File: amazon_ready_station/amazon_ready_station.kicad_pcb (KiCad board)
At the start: 2 copper layers, 35.1 x 65.2 mm, 30 parts, among them J7 BRKOUT_LEFT, J8 BRKOUT_RIGHT, Q1 2N2219

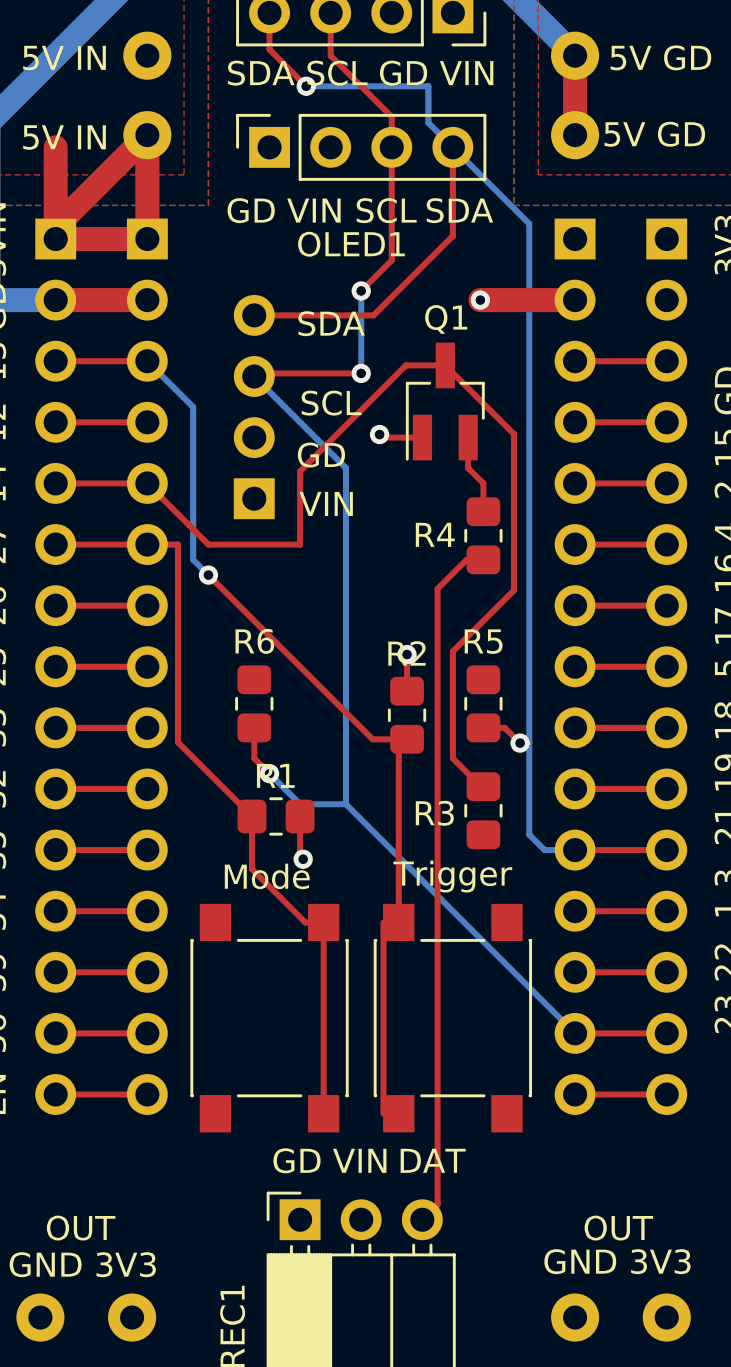
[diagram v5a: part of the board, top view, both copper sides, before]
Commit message: pcb with receiver components
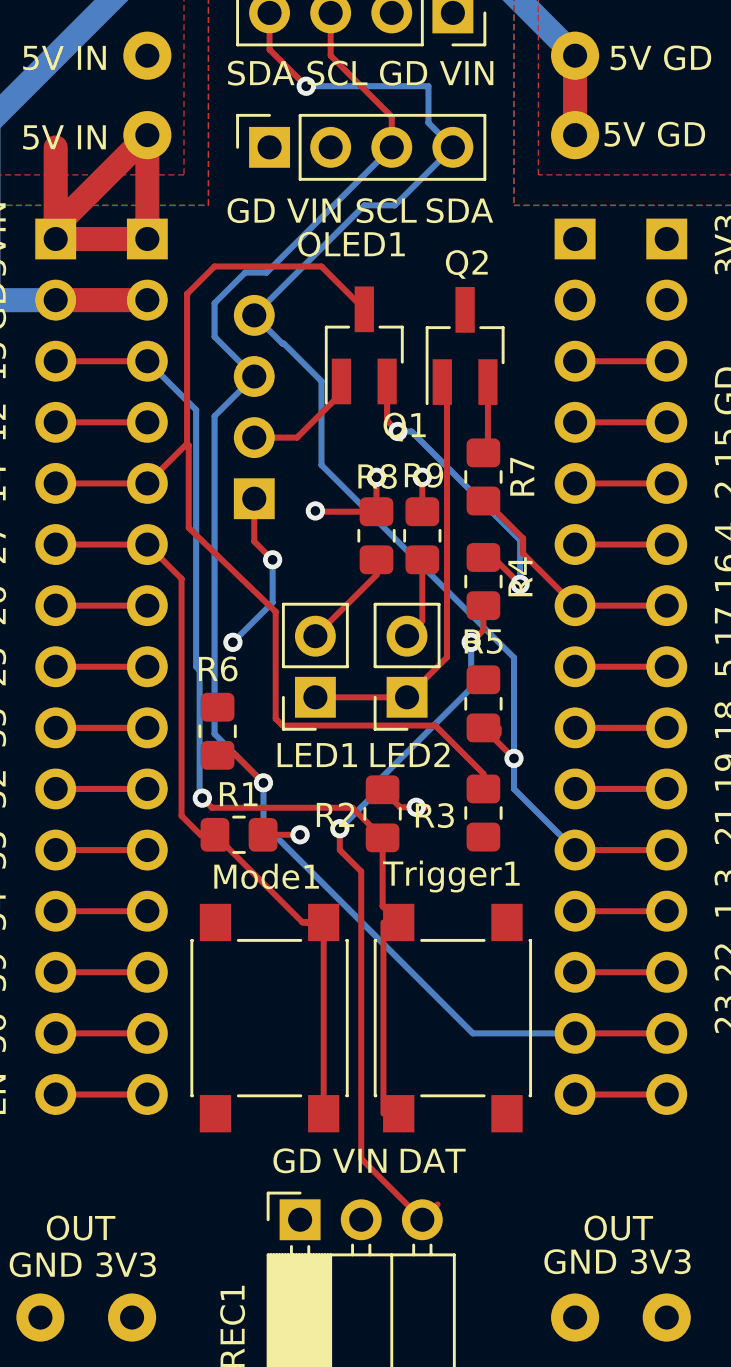
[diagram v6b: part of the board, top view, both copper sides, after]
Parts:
- added LED1: AN CAT, Connector_PinSocket_2.54mm:PinSocket_1x02_P2.54mm_Vertical, F.Cu at (168.3, 135.9)
- added LED2: ANO CAT, Connector_PinSocket_2.54mm:PinSocket_1x02_P2.54mm_Vertical, F.Cu at (172.1, 135.9)
- added Q2: 2N2219, Package_TO_SOT_SMD:SOT-23_Handsoldering, F.Cu at (174.5, 121.3)
- added R7: 100, Resistor_SMD:R_0805_2012Metric_Pad1.20x1.40mm_HandSolder, F.Cu at (175.3, 126.7)
- added R8: 220, Resistor_SMD:R_0805_2012Metric_Pad1.20x1.40mm_HandSolder, F.Cu at (170.8, 129.2)
- added R9: 220, Resistor_SMD:R_0805_2012Metric_Pad1.20x1.40mm_HandSolder, F.Cu at (172.7, 129.2)
- moved R2 4.22 mm to (171.1, 140.7)
- moved Q1 4.10 mm to (170.3, 121.3)
- moved R4 1.91 mm to (175.3, 131.1)
- moved R6 1.91 mm to (164.2, 137.3)
- moved R1 1.72 mm to (165.1, 141.6)
- moved R3 0.09 mm to (175.3, 140.7)
- renumbered Mode to Mode1, Trigger to Trigger1
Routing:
- net Net-(LED1-Pad1): track 0.00 -> 17.7 mm
- net Net-(Q1-Pad2): track 3.34 -> 13.0 mm, vias 0 -> 2
- net /3V3: track 0.00 -> 6.98 mm, vias 0 -> 2
- net /SDA: track 63.6 -> 56.9 mm
- net Net-(ESP2-Pad7): track 3.81 -> 9.79 mm
- net /GND: track 9.25 -> 13.7 mm, vias 4 -> 5
- net Net-(LED1-Pad2): track 0.00 -> 4.23 mm
- net Net-(LED2-Pad2): track 0.00 -> 3.44 mm
- net Net-(Q2-Pad2): track 0.00 -> 3.02 mm
- net Net-(ESP1-Pad3): track 40.5 -> 43.1 mm
- net Net-(IR_REC1-Pad3): track 28.9 -> 30.9 mm, vias 0 -> 2
- net Net-(ESP1-Pad5): track 42.4 -> 44.2 mm
- net /SCL: track 62.8 -> 62.7 mm, vias 3 -> 1
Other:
- board text added: "LED1"
- board text added: "LED2"
- board text added: "Remote Data Logger v1.5"
- board text removed: "Remote Data Logger v1.4"
